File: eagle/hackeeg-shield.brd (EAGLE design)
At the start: 101.6 x 53.3 mm, 145 parts, among them IC1 ADS1299IPAG, IC10 TXB0108PWR, IC11 TXB0108PWR, IC2 TPS72325DBVT, IC3 TPS73225DBVT, IC5 24AA256UID, IC6 TPS60403DBVT, IC7 OPA376DBV, IC8 OPA376DBV, IC9 TXS0102DCUR

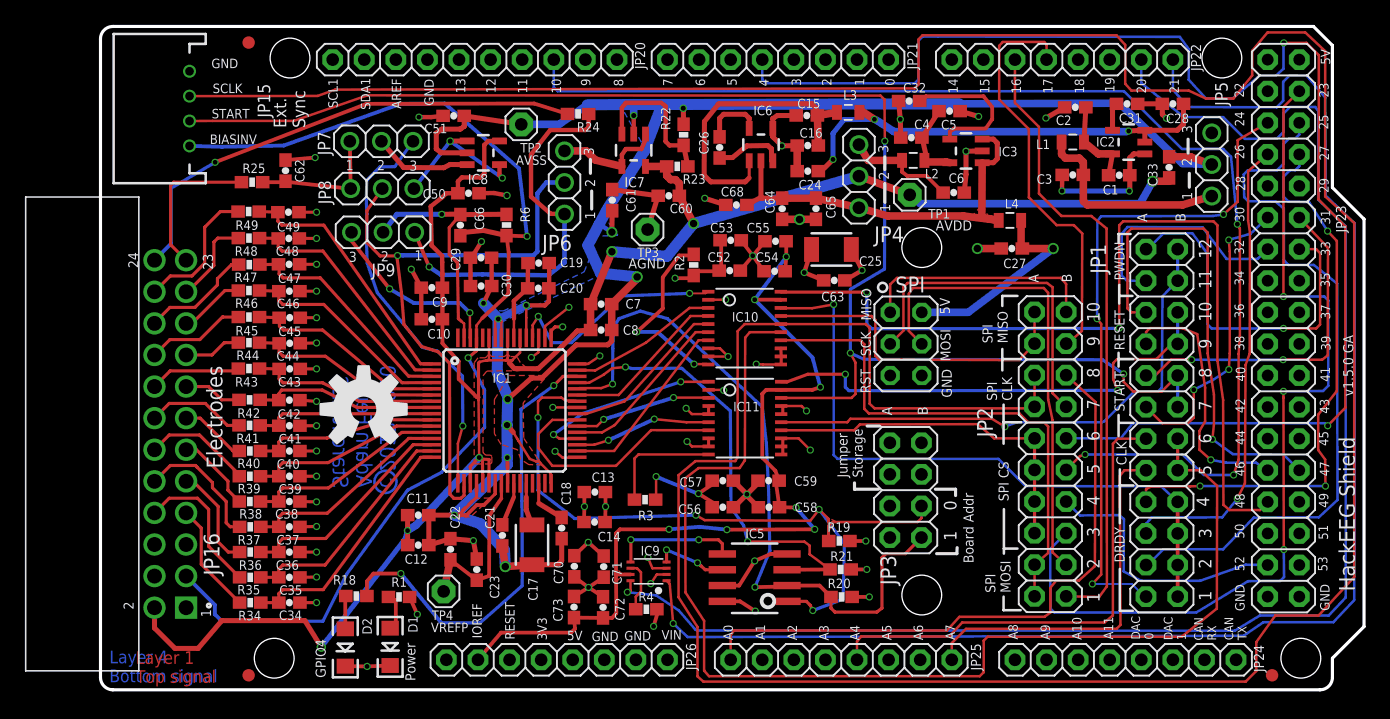
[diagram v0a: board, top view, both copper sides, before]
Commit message: Modified version that uses isolated SPI and isolated DC-DC converter (not tested much!)
To enable use of the EMG shield while the Arduino is galvanically connected to mains (in our scenario since it also containers motor driver controllers).

Basic communication works, but signal quality is not tested yet.

Issues:
- Spikes in signals, probably SPI issues
- MCU led polarity is wrong
- AIMTEC isolator doesn't fit well (keep out area is on the wrong side)
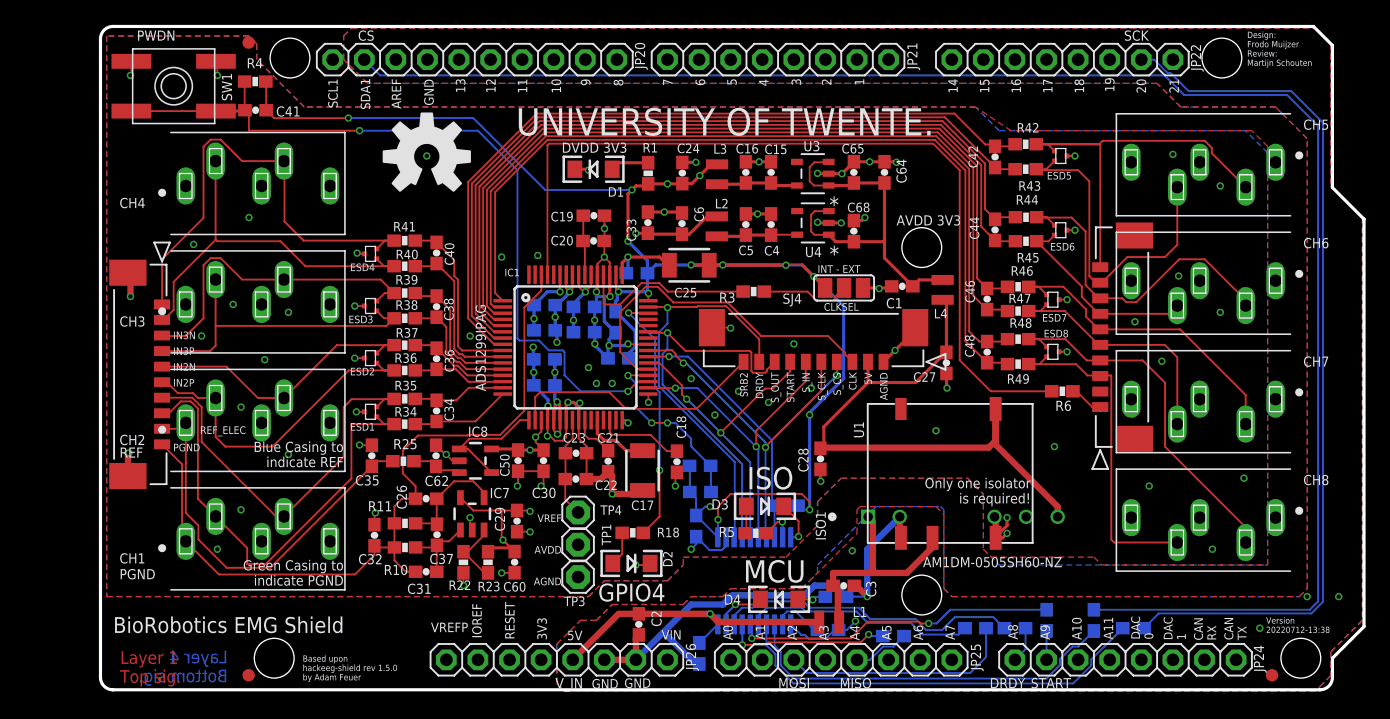
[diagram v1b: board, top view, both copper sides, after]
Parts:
- removed C43, C45, C47, C49: 4.7nF, SparkFun-Passives:0603-CAP
- removed C51, C52, C54, C56, C58, C61, C70, C72: 1uF, SparkFun-Passives:0603-CAP
- removed C53, C55, C57, C59, C71, C73: 0.1uF, SparkFun-Passives:0603-CAP
- removed C66: 0.01uF, SparkFun-Passives:0603-CAP
- removed IC10, IC11: TXB0108PWR, adafruit:TSSOP20
- removed IC2: TPS72325DBVT, TPS723xx:SOT23-5
- removed IC3: TPS73225DBVT, TPS32xx:SOT23-5
- removed IC5: 24AA256UID, microchip:SO-08
- removed IC6: TPS60403DBVT, TPS604xx:SOT23-5
- removed IC9: TXS0102DCUR, adafruit:VFSOP-8
- removed JP1: CONFIG1, headers:2X12
- removed JP15: External Sync, SparkFun-Connectors:JST-4-PTH
- removed JP16: Electrodes, OS302-R241:OST_302-R241
- removed JP2: CONFIG0, headers:2X10
- removed JP23: XIO, SmartPrj:2X18
- removed JP3: BOARD_ADDRESS, headers:2X04
- removed JP4: 5V-2.5V, headers:1X03
- removed JP5: -2.5V-GND, headers:1X03
- removed JP6: SRB1-BIAS, adafruit:1X03
- removed JP7: SRB2-REF_ELEC, adafruit:1X03
- removed JP8: SRB1-REF_ELEC, adafruit:1X03
- removed JP9: BIASOUT_BIASIN_BIAS_ELEC, headers:1X03
- removed R19, R20, R21: 10k, SparkFun-Passives:0603-RES
- removed R24: 4.99k, SparkFun-Passives:0603-RES
- removed SPI: SPI, SmartPrj:2X03
- removed TP2: AVSS_TEST_POINT, adafruit:1X01
- removed U$4: (no value), SparkFun-Aesthetics:OSHW-LOGO-L
- removed U$7: (no value), endless-knot:ENDLESSKNOT-MEDIUM
- added C67, C69: 0.1uF, SparkFun-Passives:0603-CAP
- added D3, D4: BLUE, SparkFun-LED:LED-1206
- added ESD1, ESD2, ESD3, ESD4, ESD5, ESD6, ESD7, ESD8: ESD7L, ESD7L:SOT-723
- added ISO1: AM1DM-0505SH60-NZ, Aimtec AM1D:SIP1005W50P254L1965H1265Q7
- added J1, J10, J11: 533981071, Molex Picoblade 53398-1071:CON_533981071
- added J2, J3, J4, J5, J6, J7, J8, J9: SJ1-3535N, SJ1-3535N-a:CUI_SJ1-3535N
- added R10, R11: 4.99k, SparkFun-Passives:0603-RES
- added R12, R13, R14, R15, R16, R17: 0R, SparkFun-Passives:0603-RES
- added R5, R8: 270, SparkFun-Passives:0603-RES
- added R7: 1k, SparkFun-Passives:0603-RES
- added R9: 10k, SparkFun-Passives:0603-RES
- added SJ4: CLK_SEL, jumper:SJ_2
- added SW1: SPST_TACT-EVQQ2, adafruit:EVQ-Q2
- added U1: R1SE-0505-R, R1SE-0505-R:R1SE-0505-R_RCP
- added U2: MAX14483AAP+, MAX14483AAP:21-0056C_20_MXM
- added U3, U4: ADP151AUJZ-3.3, ADP151AUJZ-3.3:UJ_5_ADI
- C1, C28: value 2.2uF -> 10uF
- C2: value 10 uF -> 4.7uF
- C26: value 1uF -> 10pF
- C29, C30: value 1uF -> 100nF
- C3: value 10uF -> 4.7uF
- C31: value 0.01uF -> 10pF
- C32: value 1uF -> 100pF
- C34, C36, C38, C40, C42, C44, C46, C48, C62: value 4.7nF -> NC
- C35: value 4.7nF -> 1 pF TVS
- C37: value 4.7nF -> 220pF
- C39, C41: value 4.7nF -> 100nF
- C4: value 2.2uF -> 1uF
- D1: value RED -> GREEN
- D2: value BLUE -> ORANGE
- L1: value 3.3 uH -> 6.8μH; device SparkFun-Passives:0805 -> SparkFun-Coils:0805-WIDE
- L2, L3, L4: value 3.3 uH -> 3.3μH; device SparkFun-Passives:0805 -> SparkFun-Coils:0805-WIDE
- R6: value 3.98K -> 4.99k
- moved C31 67.8 mm to (26.3, 9.62)
- moved R42 65.7 mm to (74.5, 44.0), turned to 180 degrees
- moved R43 64.5 mm to (74.5, 42.0), turned to 180 degrees
- moved R44 63.3 mm to (74.5, 38.1), turned to 180 degrees
- moved R49 63.1 mm to (73.9, 26.3), turned to 180 degrees
- moved R45 62.8 mm to (74.5, 36.2), turned to 180 degrees
- moved R48 62.4 mm to (73.9, 28.3), turned to 180 degrees
- moved R47 61.9 mm to (73.9, 30.6), turned to 180 degrees
- moved R46 61.8 mm to (73.9, 32.5), turned to 180 degrees
- moved C42 60.0 mm to (72.1, 43.0), turned to 270 degrees
- moved C44 57.4 mm to (72.1, 37.1), turned to 270 degrees
- moved C48 56.9 mm to (71.4, 27.3), turned to 270 degrees
- moved C46 56.1 mm to (71.4, 31.5), turned to 270 degrees
- moved C32 55.4 mm to (22.2, 12.5), turned to 270 degrees
- moved C2 54.4 mm to (43.4, 5.39), turned to 270 degrees
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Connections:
- removed net !ADC_CS_0: JP2.10, JP21.4
- removed net !ADC_CS_1: JP2.12, JP20.8
- removed net !ADC_CS_2: JP2.14, JP23.33
- removed net !ADC_CS_3: JP2.16, JP23.4
- removed net !ADC_PWDN_0: JP1.22, JP23.13
- removed net !ADC_PWDN_1: JP1.24, JP23.14
- removed net !ADC_RESET_0: JP1.18, JP23.27
- removed net !ADC_RESET_1: JP1.20, JP23.28
- removed net !ADS_PWDN: IC11.15, JP1.21, JP1.23
- removed net !ADS_RESET: IC11.20, JP1.17, JP1.19
- removed net !ADS_SPI_CS: IC11.14, JP2.11, JP2.13, JP2.15, JP2.9
- removed net +2.5V: C6.1, JP4.3, L2.2
- removed net -2.5V: C3.1, JP5.1, L1.2
- removed net ADC_CLK_0: JP1.10, JP25.8
- removed net ADC_CLK_1: JP1.12, JP25.5
- removed net ADC_DRDY_0: JP1.2, JP23.5
- removed net ADC_DRDY_1: JP1.4, JP23.6
- removed net ADC_DRDY_2: JP1.6, JP23.7
- removed net ADC_DRDY_3: JP1.8, JP23.8
- removed net ADC_START_0: JP1.14, JP23.11
- removed net ADC_START_1: JP1.16, JP23.12
- removed net ADS_CLK: IC10.15, JP1.11, JP1.9
- removed net ADS_CLKSEL: IC10.20, JP23.29
- removed net ADS_DRDY: IC10.18, JP1.1, JP1.3, JP1.5, JP1.7
- removed net ADS_SPI_CLK: IC10.16, JP15.3, JP2.5, JP2.7
- removed net ADS_SPI_IN: IC10.14, JP2.17, JP2.19
- removed net ADS_SPI_OUT: IC10.17, JP2.1, JP2.3
- removed net ADS_START: IC11.18, JP1.13, JP1.15, JP15.2
- removed net ARD_SCL: IC9.P$1, JP22.8
- removed net ARD_SDA: IC9.P$8, JP22.7
- removed net AVSS: C11.2, C12.2, C17.2, C18.2, C19.2, C20.2, C21.2, C22.2, C23.2, C29.2, C30.2, C33.2, C51.2, C61.2, C7.2, C8.2, IC1.20, IC1.23, IC1.25, IC1.32, IC1.53, IC1.57, IC1.58, IC7.2, IC8.2, JP5.2, R22.2, TP2.1
- removed net BIASIN: IC1.62, JP9.3
- removed net BIASOUT: C66.1, IC1.63, JP9.2, R6.2
- removed net BIAS_ELEC: JP6.1, JP9.1, R24.2
- removed net BIAS_ELEC_CON: JP16.24, R24.1
- removed net IOREF: C54.2, C55.2, C58.2, C59.2, C72.2, C73.2, IC10.19, IC11.19, IC9.P$7, JP26.2
- removed net N$101: JP23.15
- removed net N$102: JP23.17
- removed net N$103: JP23.19
- removed net N$104: JP23.21
- removed net N$107: JP23.23
- removed net N$108: JP23.25
- removed net N$111: JP23.31
- removed net N$24: JP21.7
- removed net N$27: JP20.3
- removed net N$28: JP20.4
- removed net N$29: JP20.5
- removed net N$30: JP20.6
- removed net N$31: JP20.7
- removed net N$33: JP20.10
- removed net N$34: JP21.1
- removed net N$35: JP21.2
- removed net N$36: JP21.3
- removed net N$37: IC9.P$6, R4.2
- removed net N$38: JP21.5
- removed net N$39: JP21.6
- removed net N$40: JP21.8
- removed net N$41: JP22.1
- removed net N$42: JP22.2
- removed net N$45: JP22.5
- removed net N$46: JP22.6
- removed net N$48: JP24.8
- removed net N$49: JP24.7
- removed net N$50: JP24.6
- removed net N$501: JP25.7
- removed net N$51: JP24.5
- removed net N$510: JP25.6
- removed net N$52: JP24.4
- removed net N$53: JP24.3
- removed net N$561: IC10.10, R2.2
- removed net N$562: IC11.10, R3.2
- removed net N$570: JP26.5
- removed net N$571: JP23.1
- removed net N$572: JP23.2
- removed net N$59: JP25.4
- removed net N$60: JP25.3
- removed net N$6001: JP20.2
- removed net N$6002: JP20.1
- removed net N$61: JP25.2
- removed net N$62: JP26.8
- removed net N$63: JP26.7
- removed net N$64: JP26.6
- removed net N$67: JP26.3
- removed net N$78: JP23.34
- removed net N$79: JP23.32
- removed net N$80: JP23.30
- removed net N$82: JP23.26
- removed net N$83: JP23.24
- removed net N$84: JP23.22
- removed net N$85: JP23.20
- removed net N$86: JP23.18
- removed net N$87: JP23.16
- removed net N$90: JP23.10
- removed net N$95: JP23.3
- removed net N$98: JP23.9
- removed net RESET: SPI.5
- removed net SCL: IC5.6, IC9.P$4
- removed net SDA: IC5.5, IC9.P$5
- removed net SPI0_MISO: JP2.2, SPI.1
- removed net SPI0_MOSI: JP2.18, SPI.4
- removed net SPI0_SCK: JP2.8, SPI.3
- removed net USART1_MISO: JP2.4, JP22.4
- removed net USART1_MOSI: JP2.20, JP22.3
- removed net USART1_SCK: JP2.6, JP25.1
- removed net VCC_-5V: C24.1, C28.1, IC2.2, IC2.3, L3.2
- new net DRDY_D69: JP24.1, R17.1
- new net N$12: R17.2, U2.18
- new net N$22: R15.2, U2.16
- new net N$23: R16.2, U2.17
- new net N$44: R7.2, U2.12
- new net PE: C2.2, C3.2, C67.2, ISO1.2, JP26.6, JP26.7, R7.1, R8.1, U1.1, U2.11
- new net PGND: C26.1, C31.1, C32.2, IC1.62, J10.10, J2.1, R10.2, R11.2
- new net SPI2_CS: JP20.2, R12.1
- new net SPI2_MISO: JP25.5, R16.1
- new net SPI2_MOSI: JP25.3, R14.1
- new net SPI2_SCK: JP22.7, R13.1
- new net START_D68: JP24.2, R15.1
- new net VCC_MCU: C2.1, C67.1, JP26.5, L1.1, U2.20
- net !PWDN: now also C41.1, R4.1, SW1.A, SW1.A'; no longer IC11.6
- net !RESET: now also C39.1, R9.1; no longer IC11.1
- net !SPI_CS: now also J1.4, R2.2, U2.8; no longer IC11.7
- net AGND: now also C11.2, C12.2, C17.2, C18.2, C19.2, C20.2, C21.2, C22.2, C23.2, C29.2, C32.1, C33.2, C35.2, C69.2, C7.2, C8.2, D3.C, ESD1.P$3, ESD2.P$3, ESD3.P$3, ESD4.P$3, ESD5.P$3, ESD6.P$3, ESD7.P$3, ESD8.P$3, IC1.20, IC1.23, IC1.25, IC1.32, IC1.53, IC1.57, IC1.58, IC7.2, IC8.2, ISO1.5, J1.1, J1.11, J1.12, J10.11, J10.12, J11.11, J11.12, R22.2, SJ4.3, SW1.B, SW1.B', U1.4, U2.10, U2.2, U3.2, U4.2; no longer C2.2, C29.1, C3.2, C31.2, C32.2, C34.2, C35.1, C36.2, C37.1, C38.2, C39.1, C40.2, C41.1, C42.2, C43.1, C44.2, C45.1, C46.2, C47.1, C48.2, C49.1, C51.1, C52.1, C53.1, C54.1, C55.1, C56.1, C57.1, C58.1, C59.1, C61.1, C70.1, C71.1, C72.1, C73.1, IC10.11, IC10.12, IC10.13, IC10.8, IC10.9, IC11.11, IC11.12, IC11.13, IC11.16, IC11.17, IC11.4, IC11.5, IC11.8, IC11.9, IC2.1, IC3.2, IC5.4, IC5.7, IC6.4, IC9.P$2, JP15.4, JP16.4, JP16.5, JP16.6, JP23.35, JP23.36, JP5.3, R19.1, R20.1, R21.1, SPI.6
- net AIN1N: now also C34.2; no longer C35.2
- net AIN2N: now also C36.2; no longer C37.2
- net AIN3N: now also C38.2; no longer C39.2
- net AIN4N: now also C40.2; no longer C41.2
- net AIN5N: now also C42.2; no longer C43.2
- net AIN6N: now also C44.2; no longer C45.2
- net AIN7N: now also C46.2; no longer C47.2
- net AIN8N: now also C48.2; no longer C49.2
- net AVDD: now also C29.1, C30.2, C6.1, L2.2; no longer JP16.2, JP4.2
- net BIASINV: now also R6.2; no longer C66.2, JP15.1, JP16.3, R6.1
- net BOARD_ADDR_0: no longer IC5.1, JP3.3, R19.2
- net BOARD_ADDR_1: no longer IC5.2, JP3.1, R20.2
- net BOARD_ADDR_2: no longer IC5.3, R21.2
- net CLK: now also J1.3; no longer IC10.6
- net CLKSEL: now also R3.1; no longer IC10.1
- net DRDY: now also J1.9, U2.3; no longer IC10.3
- net DVDD: now also C24.1, C39.2, C41.2, C69.1, L3.2, R4.2, R9.2, SJ4.1, U2.1; no longer C52.2, C53.2, C56.2, C57.2, C70.2, C71.2, IC10.2, IC11.2, IC5.8, IC9.P$3, JP16.1, JP26.4, JP3.2, JP3.4, R3.1, R4.1
- net IN1N: now also ESD1.P$2, J10.7, J2.3; no longer JP16.8
- net IN1P: now also ESD1.P$1, J10.8, J2.2; no longer JP16.7
- net IN2N: now also ESD2.P$2, J10.5, J3.3; no longer JP16.10
- net IN2P: now also ESD2.P$1, J10.6, J3.2; no longer JP16.9
- net IN3N: now also ESD3.P$2, J10.3, J4.3; no longer JP16.12
- net IN3P: now also ESD3.P$1, J10.4, J4.2; no longer JP16.11
- net IN4N: now also ESD4.P$2, J10.1, J5.3; no longer JP16.14
- net IN4P: now also ESD4.P$1, J10.2, J5.2; no longer JP16.13
- net IN5N: now also ESD5.P$2, J11.9, J6.3; no longer JP16.16
- net IN5P: now also ESD5.P$1, J11.10, J6.2; no longer JP16.15
- net IN6N: now also ESD6.P$2, J11.7, J7.3; no longer JP16.18
- net IN6P: now also ESD6.P$1, J11.8, J7.2; no longer JP16.17
- net IN7N: now also ESD7.P$2, J11.5, J8.3; no longer JP16.20
- net IN7P: now also ESD7.P$1, J11.6, J8.2; no longer JP16.19
- net IN8N: now also ESD8.P$2, J11.3, J9.3; no longer JP16.22
- net IN8P: now also ESD8.P$1, J11.4, J9.2; no longer JP16.21
- net N$1: now also U4.5; no longer IC3.5
- net N$10: now also J11.1, R6.1; no longer C26.1, IC6.3
- net N$11: now also R5.1, U2.9; no longer C32.1, IC3.4
- net N$13: now also D4.C, U2.19; no longer C31.1, IC2.4
- net N$16: now also R12.2, U2.13; no longer IC8.3, JP7.2
- net N$17: now also R13.2, U2.14; no longer IC8.1, IC8.4, JP8.3
- net N$18: now also C31.2, C37.1, R10.1; no longer IC7.4, JP6.3
- net N$2: now also C15.1, C16.1, L3.1, U3.5; no longer C1.1, C2.1, IC2.5, L1.1
- net N$20: now also R3.2, SJ4.2; no longer JP24.1
- net N$21: now also R14.2, U2.15; no longer JP26.1
- net N$54: now also C26.2, C37.2, IC7.4, R11.1; no longer JP24.2
- net N$6: now also C3.1, ISO1.1, L1.2, U1.2; no longer JP20.9
- net N$7: now also D4.A, R8.2; no longer C15.1, C16.1, IC6.1, L3.1
- net N$9: now also D3.A, R5.2; no longer C26.2, IC6.5
- net REF_ELEC: now also IC8.3; no longer JP7.1, JP8.1
- net REF_ELEC_CON: now also C35.1, J10.9, J3.1; no longer JP16.23
- net SPI_CLK: now also J1.5, U2.7; no longer IC10.5
- net SPI_IN: now also J1.6, U2.6; no longer IC10.7
- net SPI_OUT: now also J1.8, U2.4; no longer IC10.4
- net SRB1: now also IC1.17, IC8.1, IC8.4; no longer IC1.18, JP6.2, JP8.2
- net SRB2: now also IC1.18, J1.10; no longer IC1.17, JP7.3
- net START: now also J1.7, U2.5; no longer IC11.3
- net VCC_5V: now also C28.1, ISO1.7, J1.2, U1.5; no longer SPI.2
- net VCC_5V_FILTERED: now also C1.1, U3.1, U3.3, U4.1, U4.3; no longer IC3.1, IC3.3, IC6.2, JP4.1
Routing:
- net ADS_SPI_CLK: track 269.8 -> 0.00 mm
- net AVSS: track 192.2 -> 0.00 mm, vias 13 -> 0
- net SPI2_CS: track 0.00 -> 135.5 mm
- net ARD_SDA: track 120.8 -> 0.00 mm, vias 1 -> 0
- net ARD_SCL: track 119.3 -> 0.00 mm, vias 1 -> 0
- net ADS_START: track 118.6 -> 0.00 mm, vias 3 -> 0
- net AVDD: track 161.5 -> 49.2 mm, vias 6 -> 12
- net !ADC_CS_0: track 109.8 -> 0.00 mm, vias 2 -> 0
- net !ADC_CS_1: track 99.3 -> 0.00 mm, vias 3 -> 0
- net ADS_CLK: track 95.4 -> 0.00 mm
- net DVDD: track 40.9 -> 128.7 mm, vias 14 -> 15
- net IOREF: track 73.4 -> 0.00 mm, vias 7 -> 0
- net ADS_CLKSEL: track 72.9 -> 0.00 mm, vias 2 -> 0
- net !ADC_CS_3: track 72.7 -> 0.00 mm, vias 3 -> 0
- net SPI2_SCK: track 0.00 -> 70.5 mm
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- added copper zone on layer 1, net AGND
- added copper zone on layer 15, net AGND
- added copper zone on layer 16, net AGND
- added copper zone on layer 15, net AVDD
- added copper zone on layer 15, net NC
- added copper zone on layer 2, net NC
- added copper zone on layer 2, net NC1
- added copper zone on layer 2, net NC10
- added copper zone on layer 2, net NC11
- added copper zone on layer 2, net NC12
- added copper zone on layer 2, net NC13
- added copper zone on layer 2, net NC14
- added copper zone on layer 2, net NC15
- added copper zone on layer 2, net NC16
- added copper zone on layer 2, net NC17
- added copper zone on layer 2, net NC18
- added copper zone on layer 2, net NC19
- added copper zone on layer 2, net NC2
- added copper zone on layer 2, net NC20
- added copper zone on layer 2, net NC21
- added copper zone on layer 2, net NC22
- added copper zone on layer 2, net NC23
- added copper zone on layer 2, net NC24
- added copper zone on layer 2, net NC25
- added copper zone on layer 2, net NC26
- added copper zone on layer 2, net NC27
- added copper zone on layer 2, net NC28
- added copper zone on layer 2, net NC29
- added copper zone on layer 2, net NC3
- added copper zone on layer 2, net NC30
- added copper zone on layer 2, net NC31
- added copper zone on layer 2, net NC32
- added copper zone on layer 2, net NC33
- added copper zone on layer 2, net NC34
- added copper zone on layer 2, net NC35
- added copper zone on layer 2, net NC36
- added copper zone on layer 2, net NC37
- added copper zone on layer 2, net NC38
- added copper zone on layer 2, net NC39
- added copper zone on layer 2, net NC4
- added copper zone on layer 15, net NC40
- added copper zone on layer 15, net NC41
- added copper zone on layer 15, net NC42
- added copper zone on layer 15, net NC43
- added copper zone on layer 15, net NC44
- added copper zone on layer 15, net NC45
- added copper zone on layer 15, net NC46
- added copper zone on layer 15, net NC47
- added copper zone on layer 15, net NC48
- added copper zone on layer 15, net NC49
- added copper zone on layer 2, net NC5
- added copper zone on layer 15, net NC50
- added copper zone on layer 15, net NC51
- added copper zone on layer 15, net NC52
- added copper zone on layer 15, net NC53
- added copper zone on layer 15, net NC54
- added copper zone on layer 15, net NC55
- added copper zone on layer 15, net NC56
- added copper zone on layer 15, net NC57
- added copper zone on layer 15, net NC58
- added copper zone on layer 15, net NC59
- added copper zone on layer 2, net NC6
- added copper zone on layer 15, net NC60
- added copper zone on layer 15, net NC61
- added copper zone on layer 15, net NC62
- added copper zone on layer 15, net NC63
- added copper zone on layer 15, net NC64
- added copper zone on layer 15, net NC65
- added copper zone on layer 15, net NC66
- added copper zone on layer 15, net NC67
- added copper zone on layer 15, net NC68
- added copper zone on layer 15, net NC69
- added copper zone on layer 2, net NC7
- added copper zone on layer 15, net NC70
- added copper zone on layer 15, net NC71
- added copper zone on layer 15, net NC72
- added copper zone on layer 15, net NC73
- added copper zone on layer 15, net NC74
- added copper zone on layer 15, net NC75
- added copper zone on layer 15, net NC76
- added copper zone on layer 15, net NC77
- added copper zone on layer 15, net NC78
- added copper zone on layer 2, net NC8
- added copper zone on layer 2, net NC9
- added copper zone on layer 1, net PE
- added copper zone on layer 15, net PE
- added copper zone on layer 16, net PE
- added copper zone on layer 2, net PE
- removed copper zone on layer 1, net AVDD
- removed copper zone on layer 1, net AVSS
- removed copper zone on layer 16, net AVSS
- removed copper zone on layer 1, net BOARD_ADDR_0
- removed copper zone on layer 1, net IOREF
- removed copper zone on layer 2, net N$12
- removed copper zone on layer 15, net N$23
- removed copper zone on layer 1, net VCC_5V_FILTERED
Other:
- board text added: "5V_IN"
- board text added: "ADS1299IPAG"
- board text added: "AM1DM-0505SH60-NZ"
- board text added: "AVDD 3V3"
- board text added: "Based upon hackeeg-shield rev 1.5.0 by Adam Feuer"
- board text added: "BioRobotics EMG Shield"
- board text added: "Blue Casing to indicate REF"
- board text added: "CH1"
- board text added: "CH1 N P"
- board text added: "CH2"
- board text added: "CH2 N P"
- board text added: "CH3"
- board text added: "CH3 N P"
- board text added: "CH4"
- board text added: "CH4 N P"
- board text added: "CH5"
- board text added: "CH6"
- board text added: "CH7"
- board text added: "CH8"
- board text added: "CLKSEL"
- board text added: "CS"
- board text added: "DVDD 3V3"
- board text added: "Design: Frodo Muijzer Review: Martijn Schouten"
- board text added: "Green Casing to indicate PGND"
- board text added: "IN2N"
- board text added: "IN2P"
- board text added: "IN3N"
- board text added: "IN3P"
- board text added: "INT - EXT"
- board text added: "ISO"
- board text added: "ISOLATED"
- board text added: "Layer 1 Top sig."
- board text added: "Layer 3 AVDD"
- board text added: "Layer 4 Bottom sig."
- board text added: "MCU"
- board text added: "MCU Powered"
- board text added: "Only one isolator is required!"
- board text added: "Optional: R2 = SPI_CS Pull-up"
- board text added: "P N CH5"
- board text added: "P N CH6"
- board text added: "P N CH7"
- board text added: "P N CH8"
- board text added: "PE_GND"
- board text added: "PGND"
- board text added: "REF"
- board text added: "REF ELEC"
- board text added: "REF_ELEC"
- board text added: "SJ1-3535NG-BE"
- board text added: "SJ1-3535NG-GR"
- board text added: "SRB2 DRDY S_OUT START S_IN S_CLK S_CS CLK 5V AGND"
- board text added: "U1"
- board text added: "U2 SPI ISOLATOR"
- board text added: "U3"
- board text added: "U4"
- board text added: "UNIVERSITY OF TWENTE."
- board text added: "VCC_5V"
- board text added: "VREF"
- board text added: "VREF AVDD AGND"
- board text added: "V_IN"
- board text added: "Version 20220712-13:38"
- board text removed: "0"
- board text removed: "22"
- board text removed: "23"
- board text removed: "24"
- board text removed: "25"
- board text removed: "26"
- board text removed: "27"
- board text removed: "28"
- board text removed: "29"
- board text removed: "30"
- board text removed: "31"
- board text removed: "32"
- board text removed: "33"
- board text removed: "34"
- board text removed: "35"
- board text removed: "36"
- board text removed: "37"
- board text removed: "38"
- board text removed: "39"
- board text removed: "40"
- board text removed: "41"
- board text removed: "42"
- board text removed: "43"
- board text removed: "44"
- board text removed: "45"
- board text removed: "46"
- board text removed: "47"
- board text removed: "48"
- board text removed: "49"
- board text removed: "50"
- board text removed: "51"
- board text removed: "52"
- board text removed: "53"
- board text removed: "A"
- board text removed: "AVSS"
- board text removed: "B"
- board text removed: "BIASINV"
- board text removed: "Board Addr"
- board text removed: "CLK"
- board text removed: "Electrodes"
- board text removed: "Ext. Sync"
- board text removed: "HackEEG Shield"
- board text removed: "Jumper Storage"
- board text removed: "Layer 1 Top signal"
- board text removed: "Layer 3 DVDD (+)"
- board text removed: "Layer 4 Bottom signal"
- board text removed: "Power"
- board text removed: "RST"
- board text removed: "Released under the CERN Open Hardware License v.1.2"
- board text removed: "SCLK"
- board text removed: "SPI CLK"
- board text removed: "SPI CS"
- board text removed: "SPI MISO"
- board text removed: "SPI MOSI"
- board text removed: "c 2013-2020 Adam Feuer Starcat LLC"
- board text removed: "v1.5.0 GA"

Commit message: Patched led, removed header ch1 to 4, added drdy pull up
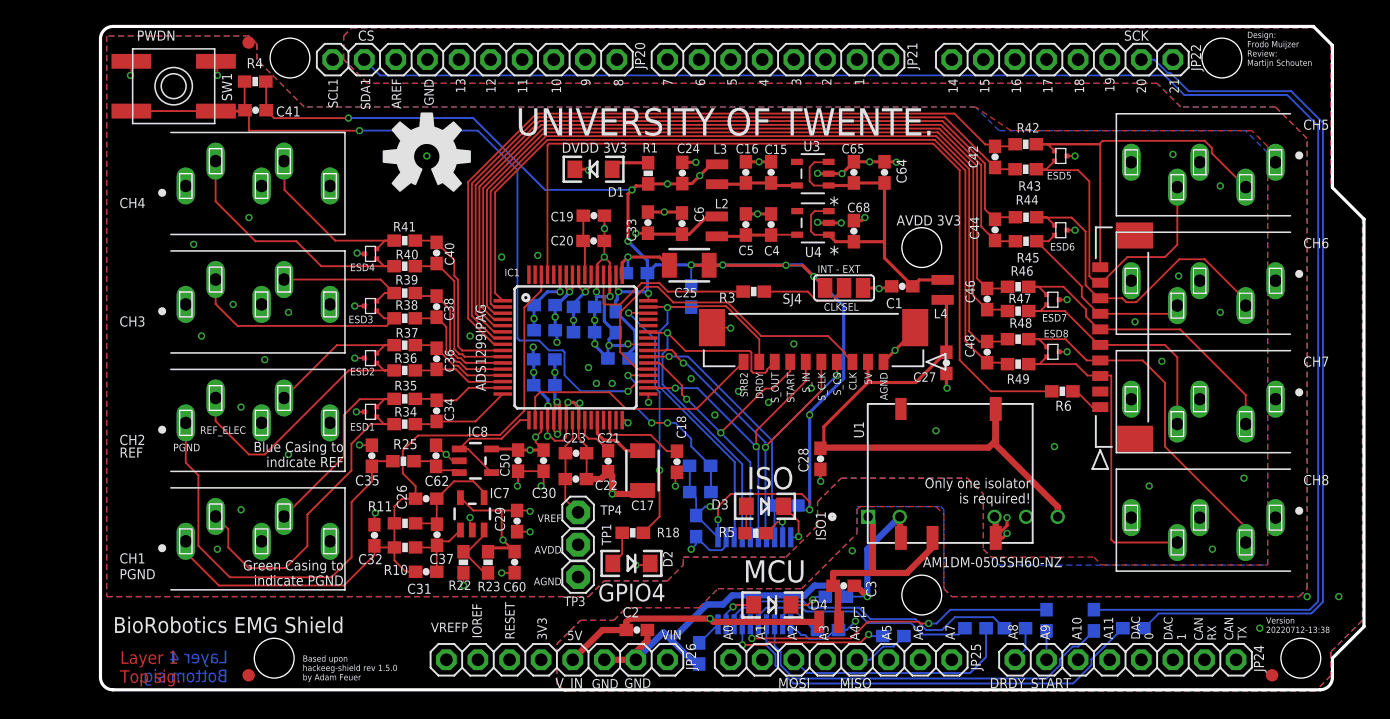
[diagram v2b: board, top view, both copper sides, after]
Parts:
- removed J10: 533981071, Molex Picoblade 53398-1071:CON_533981071
- added R19: 10k, SparkFun-Passives:0603-RES
- moved D4 0.71 mm to (54.1, 6.95), turned to 0 degrees
- moved C2 0.48 mm to (43.3, 4.93), turned to 0 degrees
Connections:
- net AGND: no longer J10.11, J10.12
- net DRDY: now also R19.2
- net DVDD: now also R19.1
- net IN1N: no longer J10.7
- net IN1P: no longer J10.8
- net IN2N: no longer J10.5
- net IN2P: no longer J10.6
- net IN3N: no longer J10.3
- net IN3P: no longer J10.4
- net IN4N: no longer J10.1
- net IN4P: no longer J10.2
- net N$13: now also R8.2; no longer U2.19
- net N$7: now also U2.19; no longer R8.2
- net PGND: no longer J10.10
- net REF_ELEC_CON: no longer J10.9
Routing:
- net IN4N: track 37.5 -> 14.5 mm
- net IN1N: track 32.2 -> 16.4 mm
- net IN3N: track 26.6 -> 11.0 mm
- net IN1P: track 38.3 -> 26.1 mm
- net IN2N: track 23.1 -> 12.3 mm
- net IN4P: track 31.5 -> 21.4 mm
- net PGND: track 63.2 -> 55.9 mm
- net IN3P: track 26.0 -> 18.9 mm
- net IN2P: track 26.8 -> 21.8 mm
- net AGND: track 136.1 -> 132.2 mm, vias 99 -> 97
- net REF_ELEC_CON: track 32.0 -> 34.3 mm
- net DRDY: track 33.2 -> 35.2 mm
- net DVDD: track 128.7 -> 130.4 mm
- net N$13: track 4.09 -> 3.04 mm
- net N$7: track 2.33 -> 3.35 mm
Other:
- board text removed: "IN2N"
- board text removed: "IN2P"
- board text removed: "IN3N"
- board text removed: "IN3P"

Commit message: added NC res/cap to potentially use the RLD
Added C and R between 61 and 63 and moved R6 closer to chip, to enable testing with RLD and future patch to enable it.
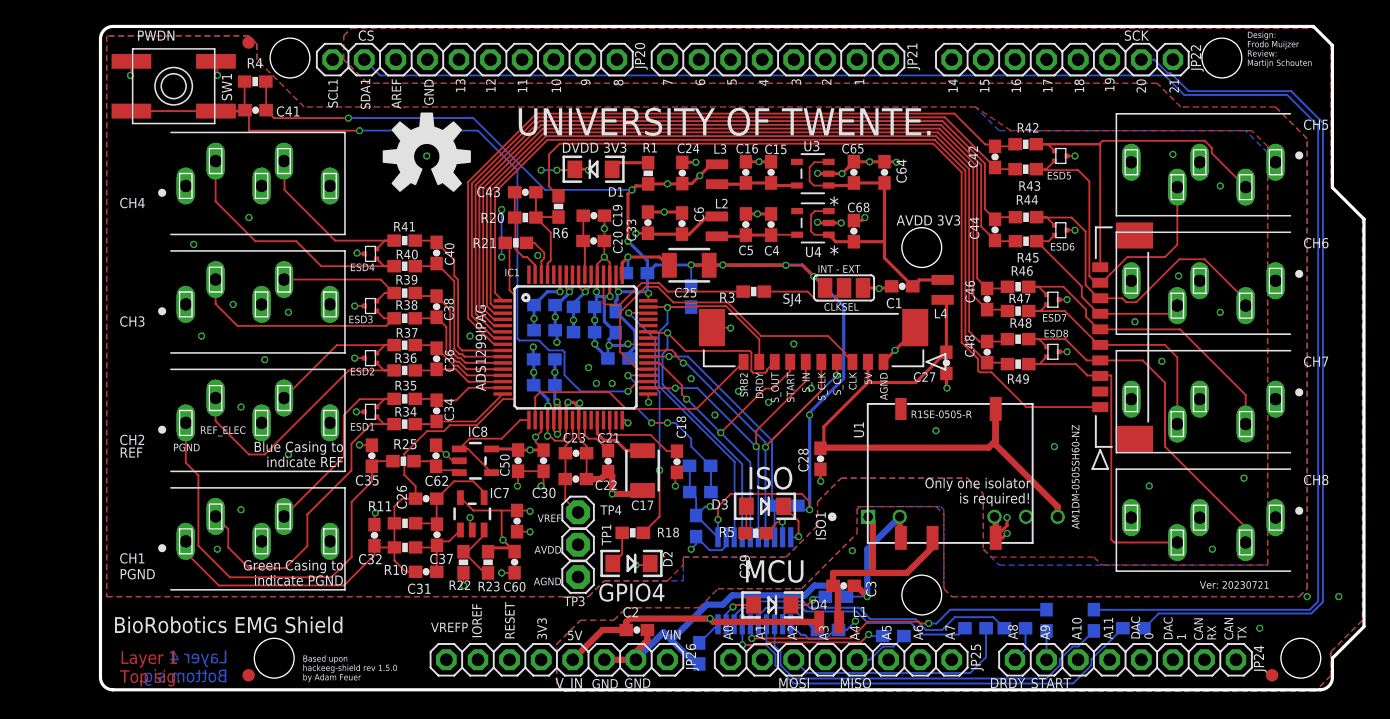
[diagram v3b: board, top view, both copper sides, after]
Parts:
- added C43: NC, SparkFun-Passives:0603-CAP
- added R20, R21: NC, SparkFun-Passives:0603-RES
- moved R6 43.2 mm to (37.0, 39.0), turned to 270 degrees
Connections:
- new net N$24: C43.1, IC1.63, R20.2
- new net N$25: IC1.62, R21.1
- net BIASINV: now also C43.2, R20.1
- net PGND: now also R21.2; no longer IC1.62
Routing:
- net N$10: track 2.72 -> 65.7 mm
- net BIASINV: track 68.2 -> 9.05 mm
- net N$24: track 0.00 -> 7.47 mm
- net AGND: track 132.2 -> 138.8 mm, vias 97 -> 100
- net N$25: track 0.00 -> 3.63 mm
- net PGND: track 55.9 -> 56.4 mm
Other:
- board text added: "R1SE-0505-R"
- board text added: "Ver: 20230721"
- board text removed: "Version 20220712-13:38"
